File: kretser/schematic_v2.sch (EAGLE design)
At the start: 16 parts, among them IC1 ATMEGA168-20PU, U2 LM2940CT-5.0/NOPB

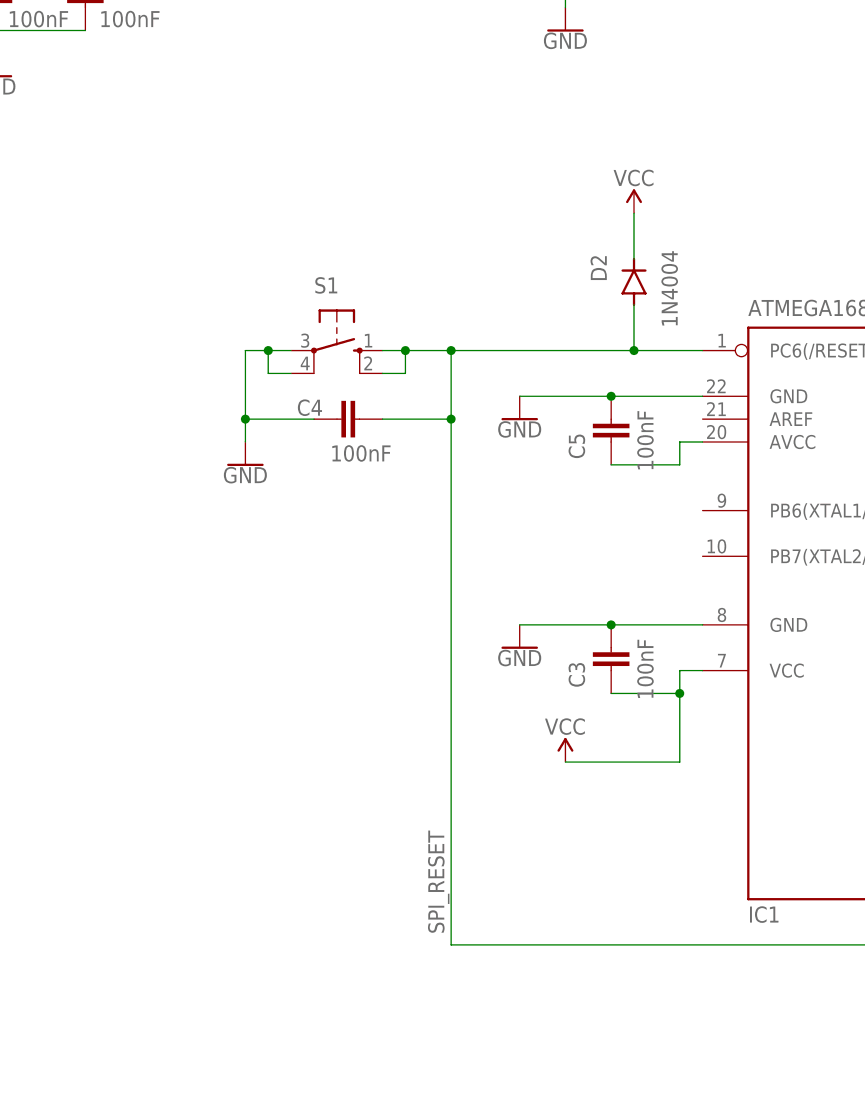
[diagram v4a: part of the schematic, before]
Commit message: Changed reset configuration to diode, capacitor, switch and series resistor.
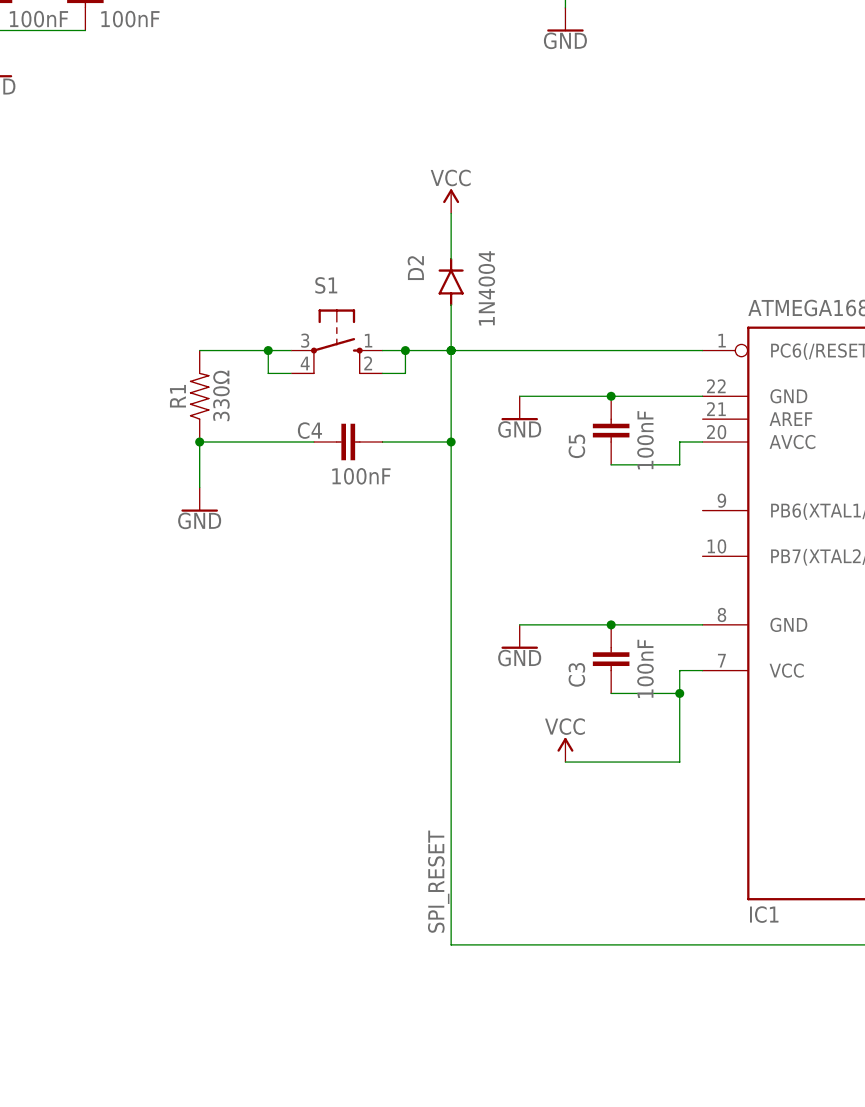
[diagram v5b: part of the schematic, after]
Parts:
- added R1: 330Ω, SparkFun-Resistors:10OHM-HORIZ-1/4W-1%
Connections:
- new net N$2: R1.2, S1.P, S1.P1
- net GND: now also R1.1; no longer S1.P, S1.P1
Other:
- moved on the sheet: C4, D2
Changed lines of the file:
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@@
 <part name="SUPPLY3" library="SparkFun-PowerSymbols" library_urn="urn:adsk.eagle:library:530" deviceset="VCC" device="" value="VCC"/>
 <part name="SUPPLY4" library="SparkFun-PowerSymbols" library_urn="urn:adsk.eagle:library:530" deviceset="VCC" device="" value="VCC"/>
+<part name="R1" library="SparkFun-Resistors" library_urn="urn:adsk.eagle:library:532" deviceset="10OHM" device="-HORIZ-1/4W-1%" package3d_urn="urn:adsk.eagle:package:39658/2" value="330Ω"/>
 </parts>
 <sheets>
@@
 <attribute name="VALUE" x="89.281" y="82.296" size="1.778" layer="96" font="vector" rot="R270"/>
 </instance>
-<instance part="GND7" gate="1" x="45.72" y="101.6" smashed="yes">
-<attribute name="VALUE" x="45.72" y="101.346" size="1.778" layer="96" font="vector" align="top-center"/>
+<instance part="GND7" gate="1" x="40.64" y="96.52" smashed="yes">
+<attribute name="VALUE" x="40.64" y="96.266" size="1.778" layer="96" font="vector" align="top-center"/>
 </instance>
 <instance part="S1" gate="1" x="55.88" y="114.3" smashed="yes" rot="R270">
@@
 <attribute name="VALUE" x="59.055" y="118.11" size="1.778" layer="96"/>
 </instance>
-<instance part="C4" gate="G$1" x="58.42" y="106.68" smashed="yes" rot="R90">
-<attribute name="NAME" x="54.356" y="108.839" size="1.778" layer="95" font="vector" rot="R180"/>
-<attribute name="VALUE" x="61.976" y="103.759" size="1.778" layer="96" font="vector" rot="R180"/>
-</instance>
-<instance part="D2" gate="1" x="88.9" y="121.92" smashed="yes" rot="R90">
-<attribute name="NAME" x="85.8774" y="121.92" size="1.778" layer="95" rot="R90"/>
-<attribute name="VALUE" x="93.7514" y="116.84" size="1.778" layer="96" rot="R90"/>
+<instance part="C4" gate="G$1" x="58.42" y="104.14" smashed="yes" rot="R90">
+<attribute name="NAME" x="54.356" y="106.299" size="1.778" layer="95" font="vector" rot="R180"/>
+<attribute name="VALUE" x="61.976" y="101.219" size="1.778" layer="96" font="vector" rot="R180"/>
+</instance>
+<instance part="D2" gate="1" x="68.58" y="121.92" smashed="yes" rot="R90">
+<attribute name="NAME" x="65.5574" y="121.92" size="1.778" layer="95" rot="R90"/>
+<attribute name="VALUE" x="73.4314" y="116.84" size="1.778" layer="96" rot="R90"/>
 </instance>
 <instance part="GND8" gate="1" x="177.8" y="71.12" smashed="yes">
@@
 <attribute name="VALUE" x="89.281" y="107.696" size="1.778" layer="96" font="vector" rot="R270"/>
 </instance>
-<instance part="SUPPLY5" gate="G$1" x="88.9" y="129.54" smashed="yes">
-<attribute name="VALUE" x="88.9" y="134.366" size="1.778" layer="96" font="vector" rot="R180" align="bottom-center"/>
+<instance part="SUPPLY5" gate="G$1" x="68.58" y="129.54" smashed="yes">
+<attribute name="VALUE" x="68.58" y="134.366" size="1.778" layer="96" font="vector" rot="R180" align="bottom-center"/>
 </instance>
 <instance part="SUPPLY2" gate="G$1" x="152.4" y="83.82" smashed="yes">
@@
 <instance part="SUPPLY4" gate="G$1" x="81.28" y="68.58" smashed="yes">
 <attribute name="VALUE" x="81.28" y="73.406" size="1.778" layer="96" font="vector" rot="R180" align="bottom-center"/>
+</instance>
+<instance part="R1" gate="G$1" x="40.64" y="109.22" smashed="yes" rot="R90">
+<attribute name="NAME" x="39.116" y="109.22" size="1.778" layer="95" font="vector" rot="R90" align="bottom-center"/>
+<attribute name="VALUE" x="42.164" y="109.22" size="1.778" layer="96" font="vector" rot="R90" align="top-center"/>
 </instance>
 </instances>
@@
 </segment>
 <segment>
-<pinref part="S1" gate="1" pin="P1"/>
-<wire x1="50.8" y1="111.76" x2="48.26" y2="111.76" width="0.1524" layer="91"/>
-<wire x1="48.26" y1="111.76" x2="48.26" y2="114.3" width="0.1524" layer="91"/>
-<pinref part="S1" gate="1" pin="P"/>
-<wire x1="48.26" y1="114.3" x2="50.8" y2="114.3" width="0.1524" layer="91"/>
-<wire x1="48.26" y1="114.3" x2="45.72" y2="114.3" width="0.1524" layer="91"/>
-<junction x="48.26" y="114.3"/>
 <pinref part="GND7" gate="1" pin="GND"/>
-<wire x1="45.72" y1="114.3" x2="45.72" y2="106.68" width="0.1524" layer="91"/>
 <pinref part="C4" gate="G$1" pin="1"/>
-<wire x1="45.72" y1="106.68" x2="45.72" y2="104.14" width="0.1524" layer="91"/>
-<wire x1="53.34" y1="106.68" x2="45.72" y2="106.68" width="0.1524" layer="91"/>
-<junction x="45.72" y="106.68"/>
+<wire x1="40.64" y1="104.14" x2="40.64" y2="99.06" width="0.1524" layer="91"/>
+<wire x1="53.34" y1="104.14" x2="40.64" y2="104.14" width="0.1524" layer="91"/>
+<pinref part="R1" gate="G$1" pin="1"/>
+<junction x="40.64" y="104.14"/>
 </segment>
 <segment>
@@
 <junction x="63.5" y="114.3"/>
 <pinref part="C4" gate="G$1" pin="2"/>
-<wire x1="60.96" y1="106.68" x2="68.58" y2="106.68" width="0.1524" layer="91"/>
-<wire x1="68.58" y1="106.68" x2="68.58" y2="114.3" width="0.1524" layer="91"/>
+<wire x1="60.96" y1="104.14" x2="68.58" y2="104.14" width="0.1524" layer="91"/>
+<wire x1="68.58" y1="104.14" x2="68.58" y2="114.3" width="0.1524" layer="91"/>
 <junction x="68.58" y="114.3"/>
 <pinref part="IC1" gate="G$1" pin="PC6(/RESET)"/>
-<wire x1="96.52" y1="114.3" x2="88.9" y2="114.3" width="0.1524" layer="91"/>
+<wire x1="96.52" y1="114.3" x2="68.58" y2="114.3" width="0.1524" layer="91"/>
 <pinref part="D2" gate="1" pin="A"/>
-<wire x1="88.9" y1="119.38" x2="88.9" y2="114.3" width="0.1524" layer="91"/>
-<wire x1="68.58" y1="114.3" x2="88.9" y2="114.3" width="0.1524" layer="91"/>
-<junction x="88.9" y="114.3"/>
-<wire x1="68.58" y1="48.26" x2="68.58" y2="106.68" width="0.1524" layer="91"/>
-<junction x="68.58" y="106.68"/>
+<wire x1="68.58" y1="119.38" x2="68.58" y2="114.3" width="0.1524" layer="91"/>
+<junction x="68.58" y="114.3"/>
+<wire x1="68.58" y1="48.26" x2="68.58" y2="104.14" width="0.1524" layer="91"/>
+<junction x="68.58" y="104.14"/>
 </segment>
 </net>
@@
 <segment>
 <pinref part="D2" gate="1" pin="C"/>
-<wire x1="88.9" y1="124.46" x2="88.9" y2="129.54" width="0.1524" layer="91"/>
+<wire x1="68.58" y1="124.46" x2="68.58" y2="129.54" width="0.1524" layer="91"/>
 <pinref part="SUPPLY5" gate="G$1" pin="VCC"/>
 </segment>
@@
 </segment>
 </net>
+<net name="N$2" class="0">
+<segment>
+<pinref part="S1" gate="1" pin="P"/>
+<pinref part="S1" gate="1" pin="P1"/>
+<wire x1="50.8" y1="111.76" x2="48.26" y2="111.76" width="0.1524" layer="91"/>
+<wire x1="48.26" y1="111.76" x2="48.26" y2="114.3" width="0.1524" layer="91"/>
+<wire x1="48.26" y1="114.3" x2="50.8" y2="114.3" width="0.1524" layer="91"/>
+<junction x="48.26" y="114.3"/>
+<wire x1="48.26" y1="114.3" x2="40.64" y2="114.3" width="0.1524" layer="91"/>
+<pinref part="R1" gate="G$1" pin="2"/>
+</segment>
+</net>

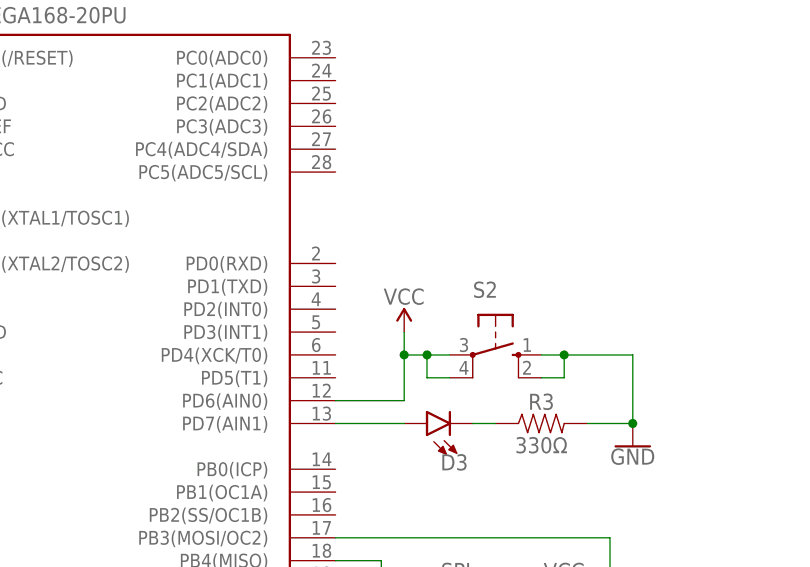
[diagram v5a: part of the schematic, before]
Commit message: Modified Reset connection and added pullup to I/O switch. Also added Sine simulation from MATLAB.
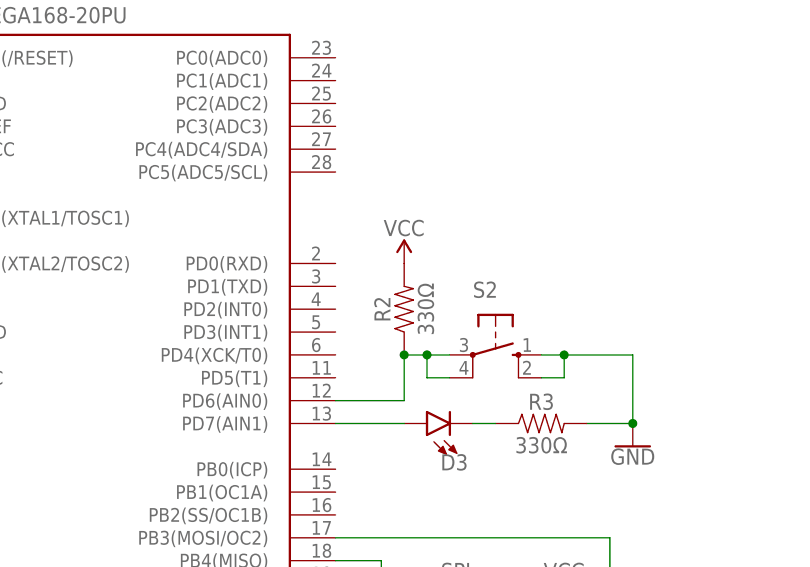
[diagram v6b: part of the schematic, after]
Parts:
- added R2: 330Ω, SparkFun-Resistors:10OHM-HORIZ-1/4W-1%
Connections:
- new net N$8: IC1.PD6(AIN0), R2.1, S2.P, S2.P1
- net VCC: now also R2.2; no longer IC1.PD6(AIN0), S2.P, S2.P1
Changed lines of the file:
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@@
 <part name="SUPPLY4" library="SparkFun-PowerSymbols" library_urn="urn:adsk.eagle:library:530" deviceset="VCC" device="" value="VCC"/>
 <part name="R1" library="SparkFun-Resistors" library_urn="urn:adsk.eagle:library:532" deviceset="10OHM" device="-HORIZ-1/4W-1%" package3d_urn="urn:adsk.eagle:package:39658/2" value="330Ω"/>
+<part name="R2" library="SparkFun-Resistors" library_urn="urn:adsk.eagle:library:532" deviceset="10OHM" device="-HORIZ-1/4W-1%" package3d_urn="urn:adsk.eagle:package:39658/2" value="330Ω"/>
 </parts>
 <sheets>
@@
 <attribute name="VALUE" x="68.58" y="134.366" size="1.778" layer="96" font="vector" rot="R180" align="bottom-center"/>
 </instance>
-<instance part="SUPPLY2" gate="G$1" x="152.4" y="83.82" smashed="yes">
-<attribute name="VALUE" x="152.4" y="88.646" size="1.778" layer="96" font="vector" rot="R180" align="bottom-center"/>
+<instance part="SUPPLY2" gate="G$1" x="152.4" y="91.44" smashed="yes">
+<attribute name="VALUE" x="152.4" y="96.266" size="1.778" layer="96" font="vector" rot="R180" align="bottom-center"/>
 </instance>
 <instance part="SUPPLY6" gate="G$1" x="170.18" y="53.34" smashed="yes">
@@
 <attribute name="NAME" x="39.116" y="109.22" size="1.778" layer="95" font="vector" rot="R90" align="bottom-center"/>
 <attribute name="VALUE" x="42.164" y="109.22" size="1.778" layer="96" font="vector" rot="R90" align="top-center"/>
+</instance>
+<instance part="R2" gate="G$1" x="152.4" y="86.36" smashed="yes" rot="R90">
+<attribute name="NAME" x="150.876" y="86.36" size="1.778" layer="95" font="vector" rot="R90" align="bottom-center"/>
+<attribute name="VALUE" x="153.924" y="86.36" size="1.778" layer="96" font="vector" rot="R90" align="top-center"/>
 </instance>
 </instances>
@@
 </segment>
 <segment>
+<pinref part="SUPPLY4" gate="G$1" pin="VCC"/>
+<pinref part="IC1" gate="G$1" pin="VCC@1"/>
+<wire x1="96.52" y1="78.74" x2="93.98" y2="78.74" width="0.1524" layer="91"/>
+<wire x1="93.98" y1="78.74" x2="93.98" y2="76.2" width="0.1524" layer="91"/>
+<pinref part="C3" gate="G$1" pin="1"/>
+<wire x1="93.98" y1="76.2" x2="86.36" y2="76.2" width="0.1524" layer="91"/>
+<wire x1="81.28" y1="68.58" x2="93.98" y2="68.58" width="0.1524" layer="91"/>
+<wire x1="93.98" y1="68.58" x2="93.98" y2="76.2" width="0.1524" layer="91"/>
+<junction x="93.98" y="76.2"/>
+</segment>
+<segment>
+<pinref part="R2" gate="G$1" pin="2"/>
+<pinref part="SUPPLY2" gate="G$1" pin="VCC"/>
+</segment>
+</net>
+<net name="N$5" class="0">
+<segment>
+<pinref part="C5" gate="G$1" pin="1"/>
+<pinref part="IC1" gate="G$1" pin="AVCC"/>
+<wire x1="96.52" y1="104.14" x2="93.98" y2="104.14" width="0.1524" layer="91"/>
+<wire x1="93.98" y1="104.14" x2="93.98" y2="101.6" width="0.1524" layer="91"/>
+<wire x1="93.98" y1="101.6" x2="86.36" y2="101.6" width="0.1524" layer="91"/>
+</segment>
+</net>
+<net name="V_IN1" class="0">
+<segment>
+<pinref part="C8" gate="G$1" pin="1"/>
+<pinref part="C7" gate="G$1" pin="1"/>
+<wire x1="27.94" y1="157.48" x2="17.78" y2="157.48" width="0.1524" layer="91"/>
+<pinref part="C6" gate="G$1" pin="1"/>
+<wire x1="17.78" y1="157.48" x2="7.62" y2="157.48" width="0.1524" layer="91"/>
+<junction x="17.78" y="157.48"/>
+<wire x1="17.78" y1="157.48" x2="17.78" y2="167.64" width="0.1524" layer="91"/>
+</segment>
+</net>
+<net name="GND1" class="0">
+<segment>
+<pinref part="C8" gate="G$1" pin="2"/>
+<pinref part="C7" gate="G$1" pin="2"/>
+<wire x1="27.94" y1="149.86" x2="17.78" y2="149.86" width="0.1524" layer="91"/>
+<wire x1="17.78" y1="149.86" x2="17.78" y2="147.32" width="0.1524" layer="91"/>
+<junction x="17.78" y="149.86"/>
+<pinref part="C6" gate="G$1" pin="2"/>
+<wire x1="17.78" y1="149.86" x2="7.62" y2="149.86" width="0.1524" layer="91"/>
+<pinref part="GND1" gate="1" pin="GND"/>
+</segment>
+</net>
+<net name="N$2" class="0">
+<segment>
+<pinref part="S1" gate="1" pin="P"/>
+<pinref part="S1" gate="1" pin="P1"/>
+<wire x1="50.8" y1="111.76" x2="48.26" y2="111.76" width="0.1524" layer="91"/>
+<wire x1="48.26" y1="111.76" x2="48.26" y2="114.3" width="0.1524" layer="91"/>
+<wire x1="48.26" y1="114.3" x2="50.8" y2="114.3" width="0.1524" layer="91"/>
+<junction x="48.26" y="114.3"/>
+<wire x1="48.26" y1="114.3" x2="40.64" y2="114.3" width="0.1524" layer="91"/>
+<pinref part="R1" gate="G$1" pin="2"/>
+</segment>
+</net>
+<net name="N$8" class="0">
+<segment>
 <pinref part="S2" gate="1" pin="P"/>
 <wire x1="154.94" y1="81.28" x2="157.48" y2="81.28" width="0.1524" layer="91"/>
@@
 <wire x1="152.4" y1="81.28" x2="152.4" y2="76.2" width="0.1524" layer="91"/>
 <junction x="154.94" y="81.28"/>
-<wire x1="152.4" y1="83.82" x2="152.4" y2="81.28" width="0.1524" layer="91"/>
+<pinref part="R2" gate="G$1" pin="1"/>
 <junction x="152.4" y="81.28"/>
-<pinref part="SUPPLY2" gate="G$1" pin="VCC"/>
-</segment>
-<segment>
-<pinref part="SUPPLY4" gate="G$1" pin="VCC"/>
-<pinref part="IC1" gate="G$1" pin="VCC@1"/>
-<wire x1="96.52" y1="78.74" x2="93.98" y2="78.74" width="0.1524" layer="91"/>
-<wire x1="93.98" y1="78.74" x2="93.98" y2="76.2" width="0.1524" layer="91"/>
-<pinref part="C3" gate="G$1" pin="1"/>
-<wire x1="93.98" y1="76.2" x2="86.36" y2="76.2" width="0.1524" layer="91"/>
-<wire x1="81.28" y1="68.58" x2="93.98" y2="68.58" width="0.1524" layer="91"/>
-<wire x1="93.98" y1="68.58" x2="93.98" y2="76.2" width="0.1524" layer="91"/>
-<junction x="93.98" y="76.2"/>
-</segment>
-</net>
-<net name="N$5" class="0">
-<segment>
-<pinref part="C5" gate="G$1" pin="1"/>
-<pinref part="IC1" gate="G$1" pin="AVCC"/>
-<wire x1="96.52" y1="104.14" x2="93.98" y2="104.14" width="0.1524" layer="91"/>
-<wire x1="93.98" y1="104.14" x2="93.98" y2="101.6" width="0.1524" layer="91"/>
-<wire x1="93.98" y1="101.6" x2="86.36" y2="101.6" width="0.1524" layer="91"/>
-</segment>
-</net>
-<net name="V_IN1" class="0">
-<segment>
-<pinref part="C8" gate="G$1" pin="1"/>
-<pinref part="C7" gate="G$1" pin="1"/>
-<wire x1="27.94" y1="157.48" x2="17.78" y2="157.48" width="0.1524" layer="91"/>
-<pinref part="C6" gate="G$1" pin="1"/>
-<wire x1="17.78" y1="157.48" x2="7.62" y2="157.48" width="0.1524" layer="91"/>
-<junction x="17.78" y="157.48"/>
-<wire x1="17.78" y1="157.48" x2="17.78" y2="167.64" width="0.1524" layer="91"/>
-</segment>
-</net>
-<net name="GND1" class="0">
-<segment>
-<pinref part="C8" gate="G$1" pin="2"/>
-<pinref part="C7" gate="G$1" pin="2"/>
-<wire x1="27.94" y1="149.86" x2="17.78" y2="149.86" width="0.1524" layer="91"/>
-<wire x1="17.78" y1="149.86" x2="17.78" y2="147.32" width="0.1524" layer="91"/>
-<junction x="17.78" y="149.86"/>
-<pinref part="C6" gate="G$1" pin="2"/>
-<wire x1="17.78" y1="149.86" x2="7.62" y2="149.86" width="0.1524" layer="91"/>
-<pinref part="GND1" gate="1" pin="GND"/>
-</segment>
-</net>
-<net name="N$2" class="0">
-<segment>
-<pinref part="S1" gate="1" pin="P"/>
-<pinref part="S1" gate="1" pin="P1"/>
-<wire x1="50.8" y1="111.76" x2="48.26" y2="111.76" width="0.1524" layer="91"/>
-<wire x1="48.26" y1="111.76" x2="48.26" y2="114.3" width="0.1524" layer="91"/>
-<wire x1="48.26" y1="114.3" x2="50.8" y2="114.3" width="0.1524" layer="91"/>
-<junction x="48.26" y="114.3"/>
-<wire x1="48.26" y1="114.3" x2="40.64" y2="114.3" width="0.1524" layer="91"/>
-<pinref part="R1" gate="G$1" pin="2"/>
-</segment>
-</net>
+</segment>
+</net>
